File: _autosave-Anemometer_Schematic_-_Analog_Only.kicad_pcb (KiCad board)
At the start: 2 copper layers, 48.8 x 53.1 mm, 48 parts, among them J1 Conn_01x10_Male, Q1 BC857, Q2 BC857, U1 LM324, U2 MAX232

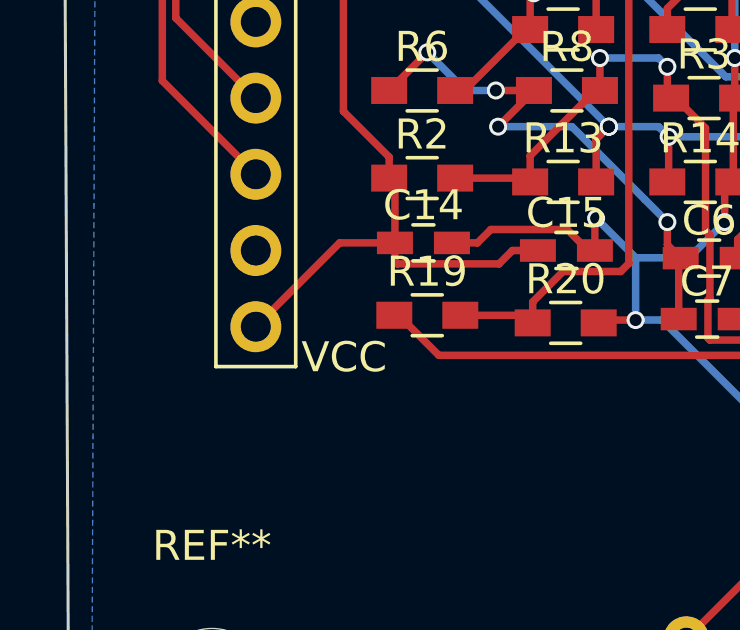
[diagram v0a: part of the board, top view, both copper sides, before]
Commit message: Updated: labeled connector on PCB
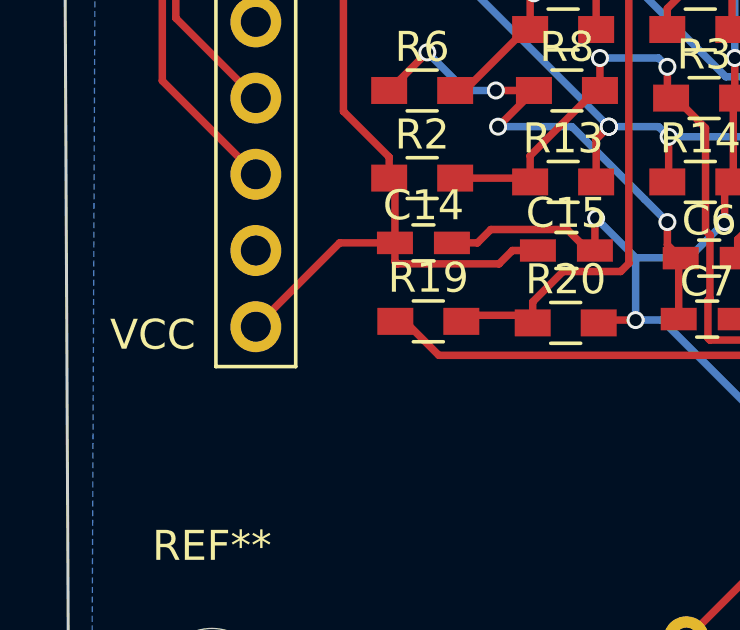
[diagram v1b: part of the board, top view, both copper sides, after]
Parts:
- moved R19 0.21 mm to (100.6, 117.7)
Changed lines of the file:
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@@
   )
   (layers
-    (0 F.Cu signal)
+    (0 F.Cu signal hide)
     (31 B.Cu signal hide)
     (32 B.Adhes user hide)
@@
     (34 B.Paste user hide)
     (35 F.Paste user)
-    (36 B.SilkS user hide)
+    (36 B.SilkS user)
     (37 F.SilkS user)
     (38 B.Mask user hide)
-    (39 F.Mask user hide)
+    (39 F.Mask user)
     (40 Dwgs.User user hide)
     (41 Cmts.User user)
@@
   )
   (module Resistors_SMD:R_0603_HandSoldering (layer F.Cu)
-    (at 100.584 117.475)
+    (at 100.61938 117.6782)
     (descr "Resistor SMD 0603, hand soldering")
     (tags "resistor 0603")
@@
     (pad 1 np_thru_hole circle (at 0 0) (size 3.5 3.5) (drill 3.5) (layers *.Cu *.Mask))
   )
-  (gr_text VCC (at 97.8154 118.87708) (layer F.SilkS)
+  (gr_text VCC (at 91.43492 118.12778) (layer F.SilkS)
     (effects (font (size 1 1) (thickness 0.25)))
   )
